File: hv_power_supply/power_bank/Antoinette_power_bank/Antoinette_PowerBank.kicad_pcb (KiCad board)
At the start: 2 copper layers, 30.5 x 48.3 mm, 44 parts, among them J1 NanoFit_RA_TH_02, J2 USB-Micro-1981568-1, J3 NanoFit_RA_TH_02, J4 USB-A-S-X-X-SM2, J5 NanoFit_RA_TH_02, Q1 SSM3K333R, U2 MCP73871T-2CCI_ML, U3 TPS61090RSAR

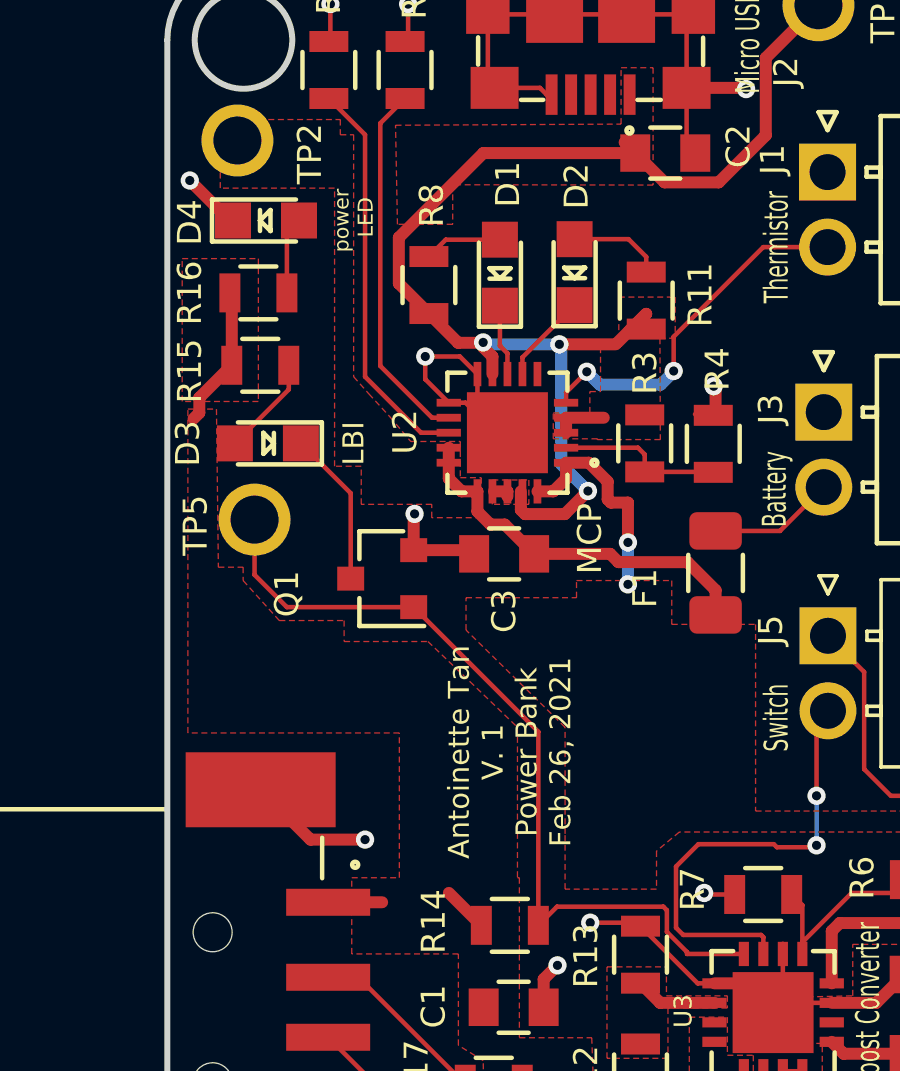
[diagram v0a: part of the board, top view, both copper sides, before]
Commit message: adjusted silkscreen to be min 0.8mm height
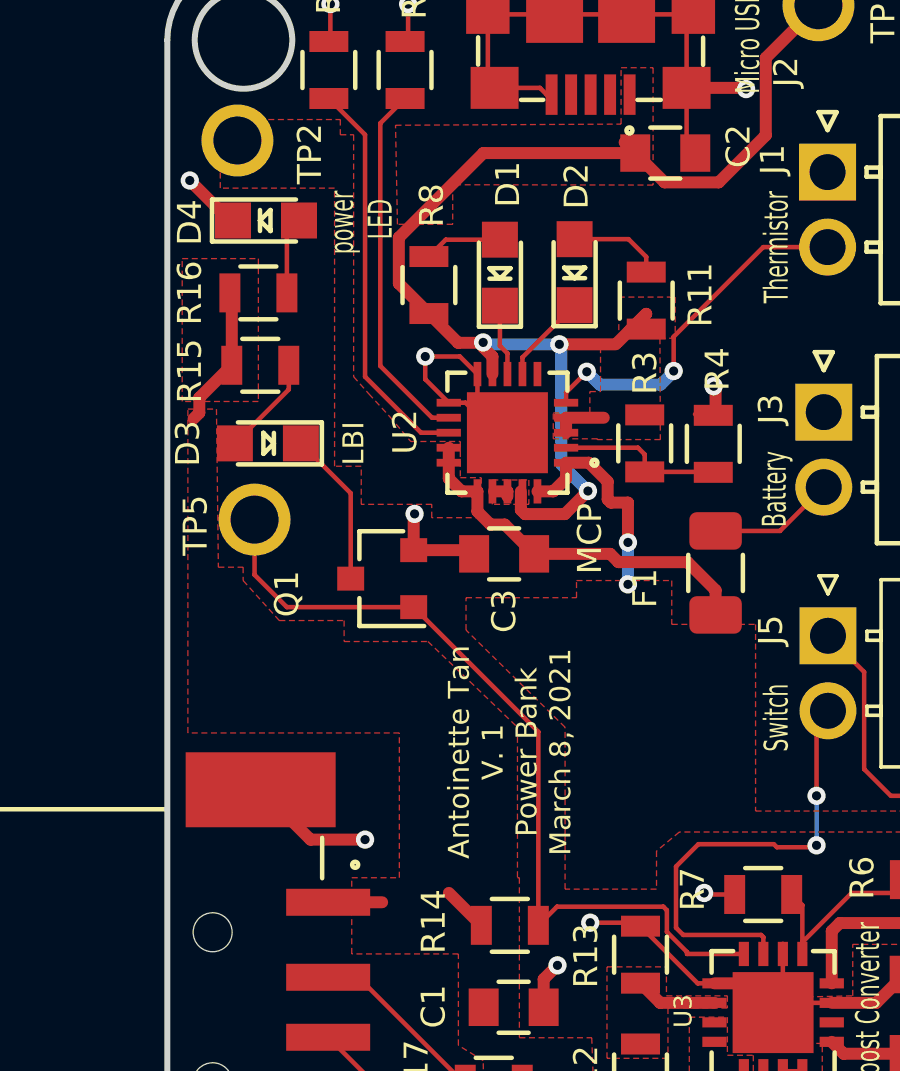
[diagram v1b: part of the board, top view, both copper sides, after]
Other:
- board text added: "Antoinette Tan V. 1 Power Bank March 8, 2021"
- board text removed: "Antoinette Tan V. 1 Power Bank Feb 26, 2021"
